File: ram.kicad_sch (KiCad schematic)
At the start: 4 parts

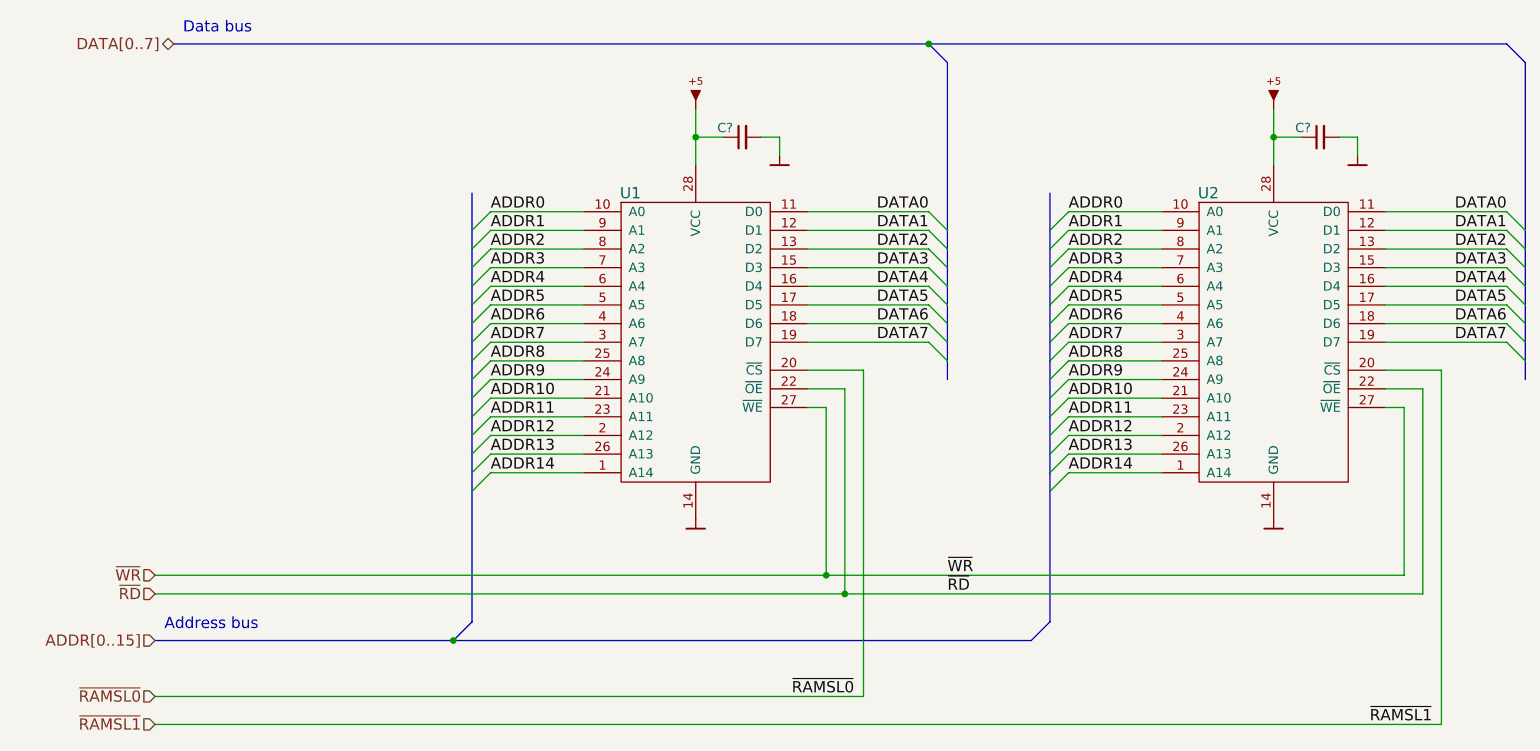
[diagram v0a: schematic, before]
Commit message: Fix wrong cap type in clock generator
Also fill some references automatically generated by KiCAD.
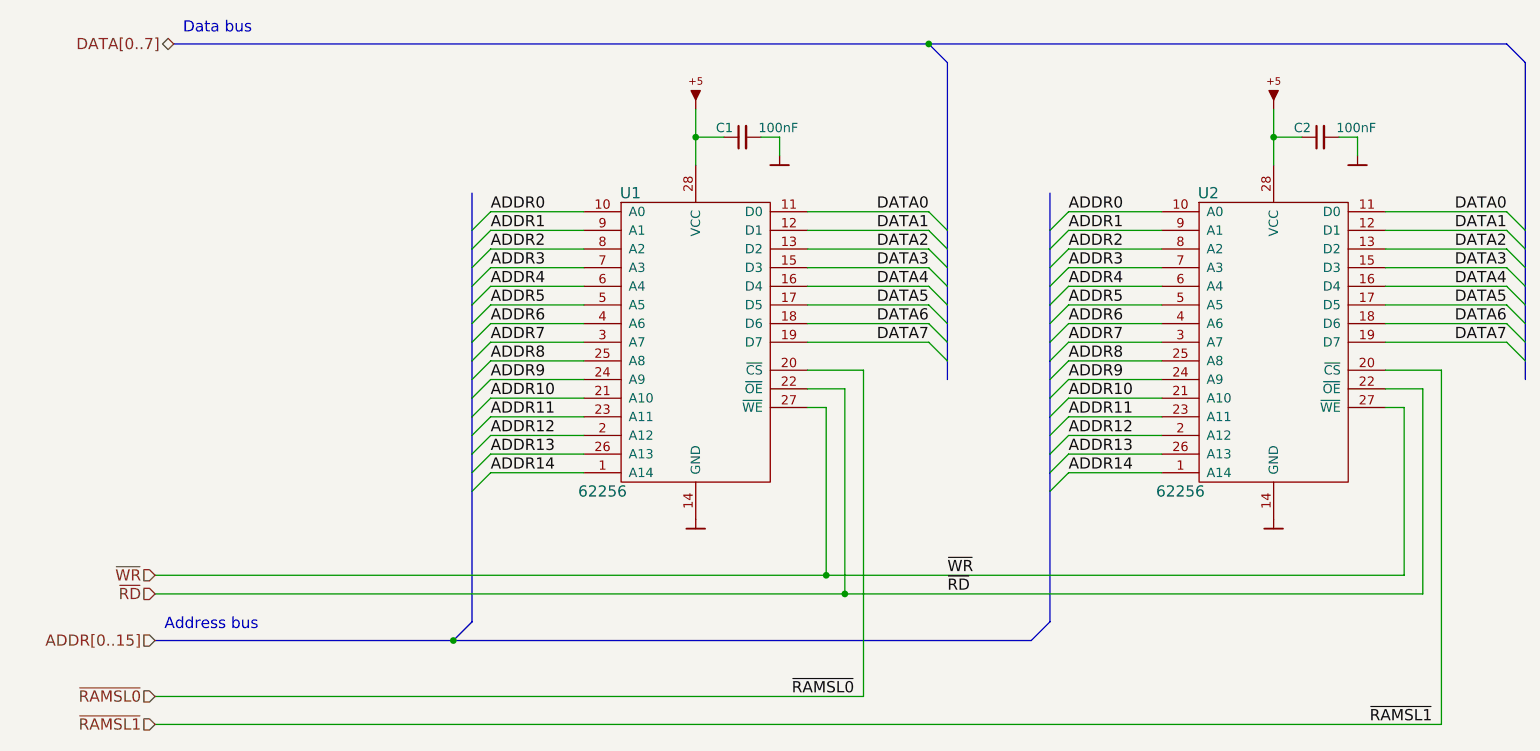
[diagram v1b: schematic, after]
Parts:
- C1, C2: renamed from C?; value (none) -> 100nF; footprint (none) -> artemisa:Disc_capacitor
- U1, U2: value (none) -> 62256; footprint (none) -> artemisa:DIP-28_600
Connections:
- net VCC: now reaches C1.1, U1.28 (VCC)
- net VCC: now also C2.1, U2.28 (VCC)
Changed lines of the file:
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@@
       (effects (font (size 1.524 1.524)))
     )
-    (property "Value" "" (id 1) (at 115.57 96.52 0)
-      (effects (font (size 1.524 1.524)))
-    )
-    (property "Footprint" "" (id 2) (at 128.27 81.28 0)
+    (property "Value" "62256" (id 1) (at 115.57 96.52 0)
+      (effects (font (size 1.524 1.524)))
+    )
+    (property "Footprint" "artemisa:DIP-28_600" (id 2) (at 128.27 81.28 0)
       (effects (font (size 1.524 1.524)) hide)
     )
@@
       (effects (font (size 1.524 1.524)))
     )
-    (property "Value" "" (id 1) (at 194.31 96.52 0)
-      (effects (font (size 1.524 1.524)))
-    )
-    (property "Footprint" "" (id 2) (at 207.01 81.28 0)
+    (property "Value" "62256" (id 1) (at 194.31 96.52 0)
+      (effects (font (size 1.524 1.524)))
+    )
+    (property "Footprint" "artemisa:DIP-28_600" (id 2) (at 207.01 81.28 0)
       (effects (font (size 1.524 1.524)) hide)
     )
@@
       (effects (font (size 1.524 1.524)) hide)
     )
-    (property "Value" "" (id 1) (at 128.27 97.79 0)
+    (property "Value" "GND" (id 1) (at 128.27 97.79 0)
       (effects (font (size 1.524 1.524)) hide)
     )
@@
       (effects (font (size 1.524 1.524)) hide)
     )
-    (property "Value" "" (id 1) (at 207.01 97.79 0)
+    (property "Value" "GND" (id 1) (at 207.01 97.79 0)
       (effects (font (size 1.524 1.524)) hide)
     )
@@
       (effects (font (size 1.524 1.524)) hide)
     )
-    (property "Value" "" (id 1) (at 128.27 38.1 0)
+    (property "Value" "VCC" (id 1) (at 128.27 38.1 0)
       (effects (font (size 1.524 1.524)) hide)
     )
@@
   (symbol (lib_id "artemisa:Cap") (at 134.62 48.26 90) (unit 1)
     (in_bom yes) (on_board yes)
-    (property "Reference" "C?" (id 0) (at 133.35 46.99 90)
-      (effects (font (size 1.27 1.27)) (justify left))
-    )
-    (property "Value" "" (id 1) (at 142.24 46.99 90)
-      (effects (font (size 1.27 1.27)) (justify left))
-    )
-    (property "Footprint" "" (id 2) (at 134.62 48.26 0)
+    (property "Reference" "C1" (id 0) (at 133.35 46.99 90)
+      (effects (font (size 1.27 1.27)) (justify left))
+    )
+    (property "Value" "100nF" (id 1) (at 142.24 46.99 90)
+      (effects (font (size 1.27 1.27)) (justify left))
+    )
+    (property "Footprint" "artemisa:Disc_capacitor" (id 2) (at 134.62 48.26 0)
       (effects (font (size 1.27 1.27)) hide)
     )
@@
       (effects (font (size 1.524 1.524)) hide)
     )
-    (property "Value" "" (id 1) (at 139.7 48.26 0)
+    (property "Value" "GND" (id 1) (at 139.7 48.26 0)
       (effects (font (size 1.524 1.524)) hide)
     )
@@
       (effects (font (size 1.524 1.524)) hide)
     )
-    (property "Value" "" (id 1) (at 207.01 38.1 0)
+    (property "Value" "VCC" (id 1) (at 207.01 38.1 0)
       (effects (font (size 1.524 1.524)) hide)
     )
@@
   (symbol (lib_id "artemisa:Cap") (at 213.36 48.26 90) (unit 1)
     (in_bom yes) (on_board yes)
-    (property "Reference" "C?" (id 0) (at 212.09 46.99 90)
-      (effects (font (size 1.27 1.27)) (justify left))
-    )
-    (property "Value" "" (id 1) (at 220.98 46.99 90)
-      (effects (font (size 1.27 1.27)) (justify left))
-    )
-    (property "Footprint" "" (id 2) (at 213.36 48.26 0)
+    (property "Reference" "C2" (id 0) (at 212.09 46.99 90)
+      (effects (font (size 1.27 1.27)) (justify left))
+    )
+    (property "Value" "100nF" (id 1) (at 220.98 46.99 90)
+      (effects (font (size 1.27 1.27)) (justify left))
+    )
+    (property "Footprint" "artemisa:Disc_capacitor" (id 2) (at 213.36 48.26 0)
       (effects (font (size 1.27 1.27)) hide)
     )
@@
       (effects (font (size 1.524 1.524)) hide)
     )
-    (property "Value" "" (id 1) (at 218.44 48.26 0)
-      (effects (font (size 1.524 1.524)) hide)
-    )
+    (property "Value" "GND" (id 1) (at 218.44 48.26 0)
+      (effects (font (size 1.524 1.524)) hide)
+    )
